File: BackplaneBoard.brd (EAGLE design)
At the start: 139.7 x 79.9 mm, 4 parts

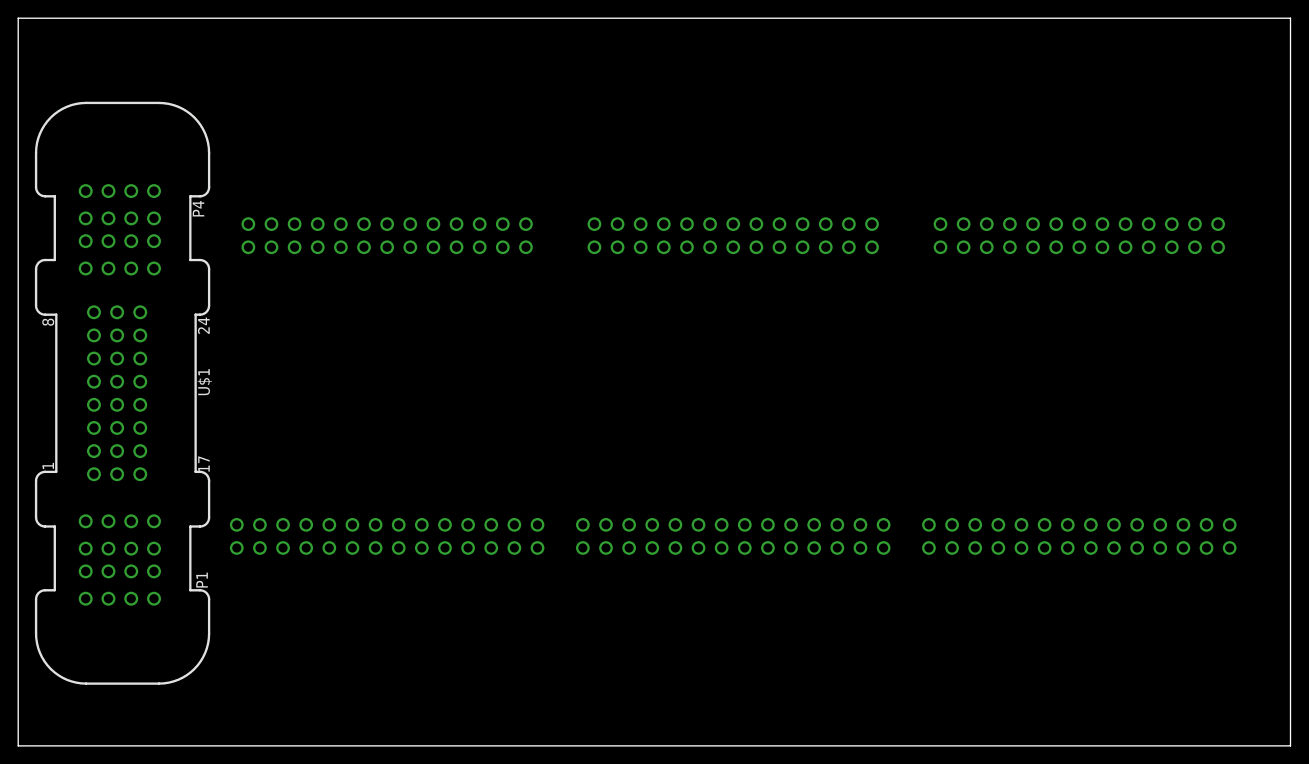
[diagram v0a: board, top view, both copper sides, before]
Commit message: moved some connectors
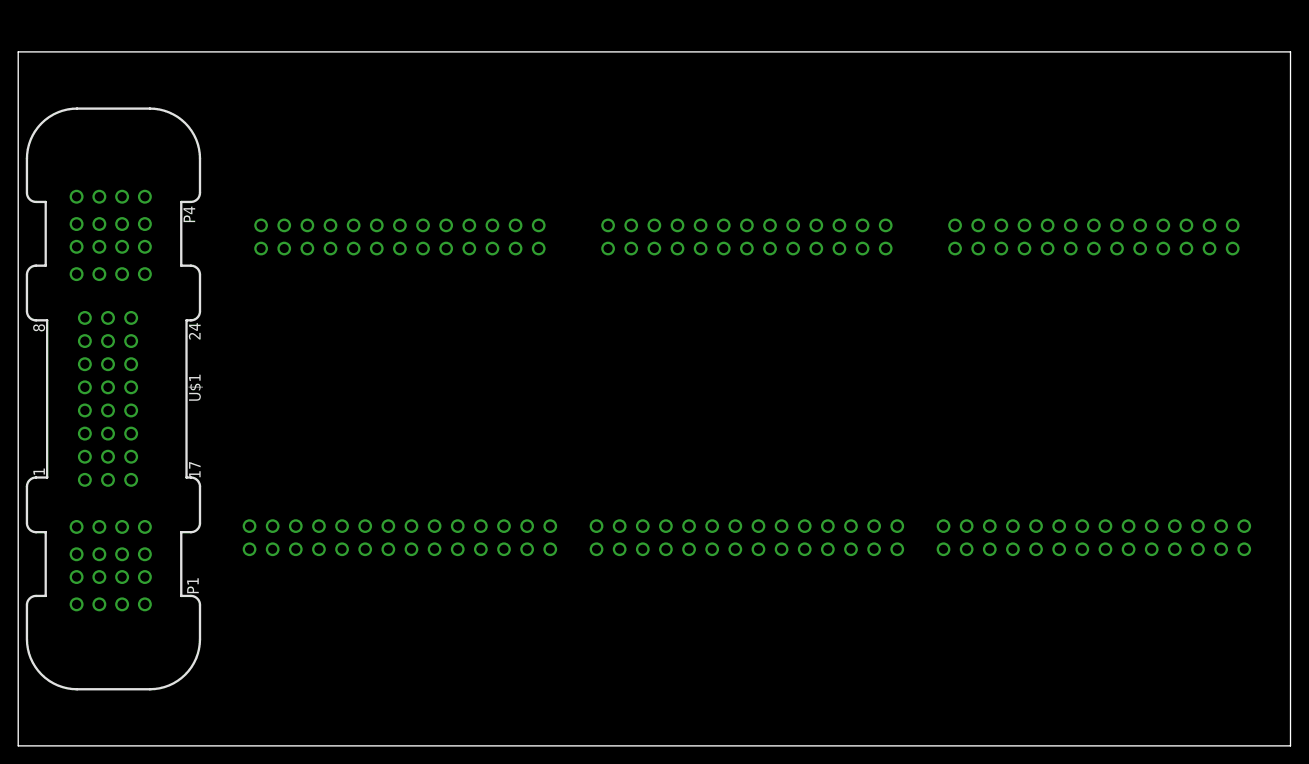
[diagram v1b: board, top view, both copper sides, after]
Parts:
- moved U$4 1.61 mm to (101.6, 22.9)
- moved U$3 1.51 mm to (63.5, 22.9)
- moved U$2 1.41 mm to (25.4, 22.9)
- moved U$1 1.18 mm to (10.2, 38.1)
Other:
- board size 139.7 x 79.9 mm -> 139.7 x 76.2 mm
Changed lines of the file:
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@@
 <setting verticaltext="up"/>
 </settings>
-<grid distance="1" unitdist="mm" unit="mm" style="lines" multiple="1" display="no" altdistance="5" altunitdist="mil" altunit="mil"/>
+<grid distance="1" unitdist="inch" unit="inch" style="lines" multiple="1" display="no" altdistance="5" altunitdist="mil" altunit="mil"/>
 <layers>
 <layer number="1" name="Top" color="4" fill="1" visible="yes" active="yes"/>
@@
 <plain>
 <wire x1="0" y1="0" x2="139.7" y2="0" width="0" layer="20"/>
-<wire x1="139.7" y1="0" x2="139.7" y2="79.9" width="0" layer="20"/>
-<wire x1="139.7" y1="79.9" x2="0" y2="79.9" width="0" layer="20"/>
-<wire x1="0" y1="79.9" x2="0" y2="0" width="0" layer="20"/>
+<wire x1="139.7" y1="0" x2="139.7" y2="76.2" width="0" layer="20"/>
+<wire x1="139.7" y1="76.2" x2="0" y2="76.2" width="0" layer="20"/>
+<wire x1="0" y1="76.2" x2="0" y2="0" width="0" layer="20"/>
 </plain>
 <attributes>
@@
 </autorouter>
 <elements>
-<element name="U$1" library="ET60S-02-24-02-X-VP-GP" package="ET60S-02-24-02-X-VP-GP" value="ET60S-02-24-02-X-VP-GP" x="11.16" y="38.72" rot="R270">
-<attribute name="NAME" x="19.76" y="41.52" size="1.27" layer="25" rot="R270"/>
-<attribute name="VALUE" x="2.56" y="41.52" size="1.27" layer="27" rot="R270"/>
+<element name="U$1" library="ET60S-02-24-02-X-VP-GP" package="ET60S-02-24-02-X-VP-GP" value="ET60S-02-24-02-X-VP-GP" x="10.16" y="38.1" rot="R270">
+<attribute name="NAME" x="18.76" y="40.9" size="1.27" layer="25" rot="R270"/>
+<attribute name="VALUE" x="1.56" y="40.9" size="1.27" layer="27" rot="R270"/>
 </element>
-<element name="U$2" library="ESC_to_Backplane_Connectors" package="ESC2BACKPLANE_WHOLE" value="ESC2BACKPLANE" x="24" y="23"/>
-<element name="U$3" library="ESC_to_Backplane_Connectors" package="ESC2BACKPLANE_WHOLE" value="ESC2BACKPLANE" x="62" y="23"/>
-<element name="U$4" library="ESC_to_Backplane_Connectors" package="ESC2BACKPLANE_WHOLE" value="ESC2BACKPLANE" x="100" y="23"/>
+<element name="U$2" library="ESC_to_Backplane_Connectors" package="ESC2BACKPLANE_WHOLE" value="ESC2BACKPLANE" x="25.4" y="22.86"/>
+<element name="U$3" library="ESC_to_Backplane_Connectors" package="ESC2BACKPLANE_WHOLE" value="ESC2BACKPLANE" x="63.5" y="22.86"/>
+<element name="U$4" library="ESC_to_Backplane_Connectors" package="ESC2BACKPLANE_WHOLE" value="ESC2BACKPLANE" x="101.6" y="22.86"/>
 </elements>
 <signals>

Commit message: added holes for standoffs
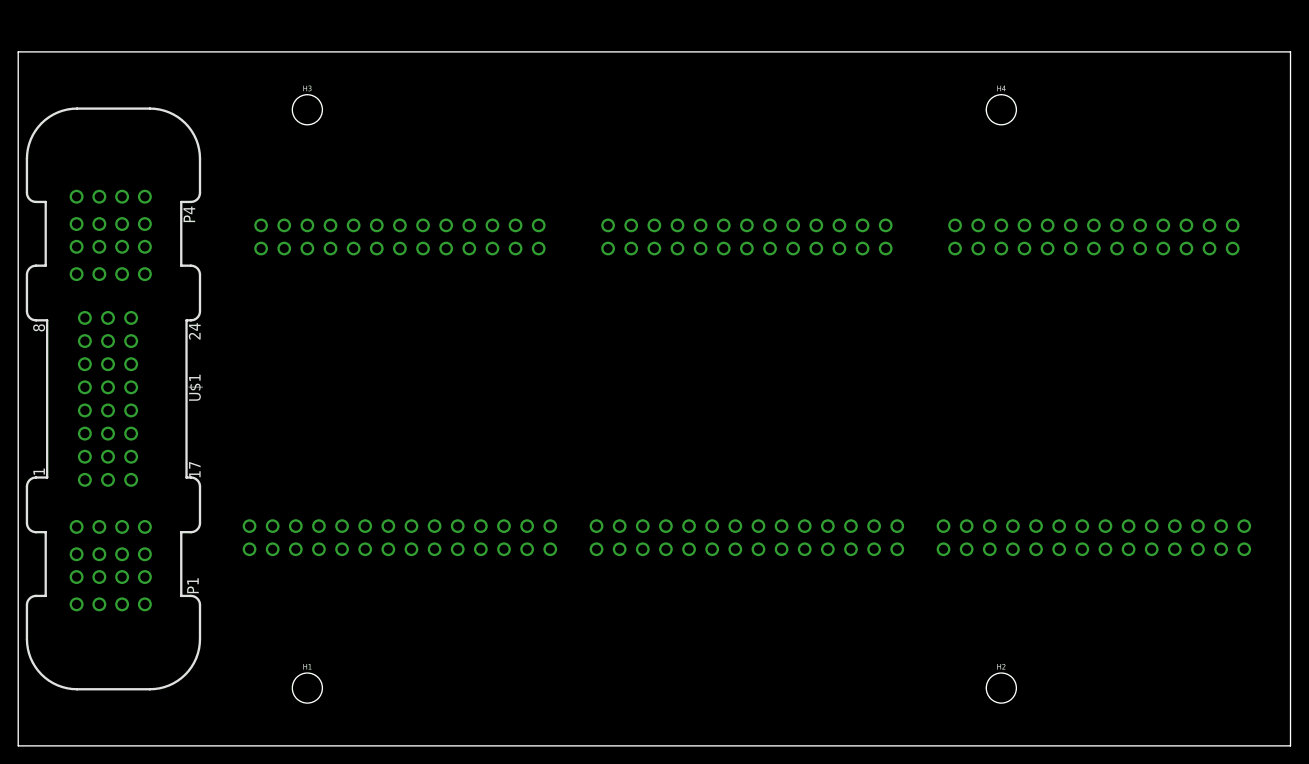
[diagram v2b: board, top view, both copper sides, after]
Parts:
- added H1, H2, H3, H4: STAND-OFF, SparkFun-Hardware:STAND-OFF
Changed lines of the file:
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@@
 <setting verticaltext="up"/>
 </settings>
-<grid distance="1" unitdist="inch" unit="inch" style="lines" multiple="1" display="no" altdistance="5" altunitdist="mil" altunit="mil"/>
+<grid distance="0.75" unitdist="inch" unit="inch" style="lines" multiple="1" display="no" altdistance="5" altunitdist="mil" altunit="mil"/>
 <layers>
 <layer number="1" name="Top" color="4" fill="1" visible="yes" active="yes"/>
+<layer number="2" name="Route2" color="1" fill="3" visible="yes" active="yes"/>
+<layer number="3" name="Route3" color="4" fill="3" visible="yes" active="yes"/>
+<layer number="4" name="Route4" color="1" fill="4" visible="yes" active="yes"/>
+<layer number="5" name="Route5" color="4" fill="4" visible="yes" active="yes"/>
+<layer number="6" name="Route6" color="1" fill="8" visible="yes" active="yes"/>
+<layer number="7" name="Route7" color="4" fill="8" visible="yes" active="yes"/>
+<layer number="8" name="Route8" color="1" fill="2" visible="yes" active="yes"/>
+<layer number="9" name="Route9" color="4" fill="2" visible="yes" active="yes"/>
+<layer number="10" name="Route10" color="1" fill="7" visible="yes" active="yes"/>
+<layer number="11" name="Route11" color="4" fill="7" visible="yes" active="yes"/>
+<layer number="12" name="Route12" color="1" fill="5" visible="yes" active="yes"/>
+<layer number="13" name="Route13" color="4" fill="5" visible="yes" active="yes"/>
+<layer number="14" name="Route14" color="1" fill="6" visible="yes" active="yes"/>
+<layer number="15" name="Route15" color="4" fill="6" visible="yes" active="yes"/>
 <layer number="16" name="Bottom" color="1" fill="1" visible="yes" active="yes"/>
 <layer number="17" name="Pads" color="2" fill="1" visible="yes" active="yes"/>
@@
 <layer number="112" name="tSilk" color="7" fill="1" visible="yes" active="yes"/>
 <layer number="113" name="IDFDebug" color="7" fill="1" visible="yes" active="yes"/>
+<layer number="114" name="Badge_Outline" color="7" fill="1" visible="yes" active="yes"/>
 <layer number="116" name="Patch_BOT" color="9" fill="4" visible="yes" active="yes"/>
 <layer number="118" name="Rect_Pads" color="7" fill="1" visible="yes" active="yes"/>
@@
 <element name="U$3" library="ESC_to_Backplane_Connectors" package="ESC2BACKPLANE_WHOLE" value="ESC2BACKPLANE" x="63.5" y="22.86"/>
 <element name="U$4" library="ESC_to_Backplane_Connectors" package="ESC2BACKPLANE_WHOLE" value="ESC2BACKPLANE" x="101.6" y="22.86"/>
+<element name="H1" library="SparkFun-Hardware" library_urn="urn:adsk.eagle:library:519" package="STAND-OFF" package3d_urn="urn:adsk.eagle:package:38630/1" value="STAND-OFF" x="31.75" y="6.35">
+<attribute name="NAME" x="31.75" y="8.382" size="0.6096" layer="25" font="vector" ratio="20" align="bottom-center"/>
+<attribute name="VALUE" x="31.75" y="4.318" size="0.6096" layer="27" font="vector" ratio="20" align="top-center"/>
+</element>
+<element name="H2" library="SparkFun-Hardware" library_urn="urn:adsk.eagle:library:519" package="STAND-OFF" package3d_urn="urn:adsk.eagle:package:38630/1" value="STAND-OFF" x="107.95" y="6.35">
+<attribute name="NAME" x="107.95" y="8.382" size="0.6096" layer="25" font="vector" ratio="20" align="bottom-center"/>
+<attribute name="VALUE" x="107.95" y="4.318" size="0.6096" layer="27" font="vector" ratio="20" align="top-center"/>
+</element>
+<element name="H3" library="SparkFun-Hardware" library_urn="urn:adsk.eagle:library:519" package="STAND-OFF" package3d_urn="urn:adsk.eagle:package:38630/1" value="STAND-OFF" x="31.75" y="69.85">
+<attribute name="NAME" x="31.75" y="71.882" size="0.6096" layer="25" font="vector" ratio="20" align="bottom-center"/>
+<attribute name="VALUE" x="31.75" y="67.818" size="0.6096" layer="27" font="vector" ratio="20" align="top-center"/>
+</element>
+<element name="H4" library="SparkFun-Hardware" library_urn="urn:adsk.eagle:library:519" package="STAND-OFF" package3d_urn="urn:adsk.eagle:package:38630/1" value="STAND-OFF" x="107.95" y="69.85">
+<attribute name="NAME" x="107.95" y="71.882" size="0.6096" layer="25" font="vector" ratio="20" align="bottom-center"/>
+<attribute name="VALUE" x="107.95" y="67.818" size="0.6096" layer="27" font="vector" ratio="20" align="top-center"/>
+</element>
 </elements>
 <signals>
@@
 </board>
 </drawing>
+<compatibility>
+<note version="8.2" severity="warning">
+Since Version 8.2, EAGLE supports online libraries. The ids
+of those online libraries will not be understood (or retained)
+with this version.
+</note>
+<note version="8.3" severity="warning">
+Since Version 8.3, EAGLE supports URNs for individual library
+assets (packages, symbols, and devices). The URNs of those assets
+will not be understood (or retained) with this version.
+</note>
+<note version="8.3" severity="warning">
+Since Version 8.3, EAGLE supports the association of 3D packages
+with devices in libraries, schematics, and board files. Those 3D
+packages will not be understood (or retained) with this version.
+</note>
+</compatibility>
 </eagle>

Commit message: Netted and labeled pins
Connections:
- new net +12V: U$2.P$10, U$2.P$11, U$2.P$12, U$2.P$13, U$2.P$23, U$2.P$9, U$2.P$A, U$2.P$B, U$2.P$C, U$2.P$D, U$2.P$E, U$2.P$O, U$2.P$P, U$2.P$Q, U$2.P$R, U$2.P$S, U$3.P$10, U$3.P$11, U$3.P$12, U$3.P$13, U$3.P$23, U$3.P$24, U$3.P$25, U$3.P$26, U$3.P$27, U$3.P$9, U$3.P$A, U$3.P$B, U$3.P$C, U$3.P$D, U$3.P$E, U$3.P$O, U$3.P$P, U$3.P$Q, U$3.P$R, U$3.P$S, U$4.P$10, U$4.P$11, U$4.P$12, U$4.P$13, U$4.P$23, U$4.P$24, U$4.P$25, U$4.P$26, U$4.P$27, U$4.P$9, U$4.P$A, U$4.P$B, U$4.P$C, U$4.P$D, U$4.P$E, U$4.P$O, U$4.P$P, U$4.P$Q, U$4.P$R, U$4.P$S
- new net +3V3: U$2.P$G, U$2.P$H, U$2.P$U, U$2.P$V, U$3.P$G, U$3.P$H, U$3.P$U, U$3.P$V, U$4.P$G, U$4.P$H, U$4.P$U, U$4.P$V
- new net CAN_H: U$2.P$6, U$3.P$6, U$4.P$6
- new net CAN_L: U$2.P$7, U$3.P$7, U$4.P$7
- new net GND: U$2.P$1, U$2.P$15, U$2.P$16, U$2.P$17, U$2.P$18, U$2.P$2, U$2.P$3, U$2.P$4, U$2.P$AA, U$2.P$BB, U$2.P$J, U$2.P$K, U$2.P$L, U$2.P$M, U$2.P$N, U$2.P$X, U$2.P$Y, U$2.P$Z, U$3.P$1, U$3.P$15, U$3.P$16, U$3.P$17, U$3.P$18, U$3.P$2, U$3.P$3, U$3.P$4, U$3.P$AA, U$3.P$BB, U$3.P$J, U$3.P$K, U$3.P$L, U$3.P$M, U$3.P$N, U$3.P$X, U$3.P$Y, U$3.P$Z, U$4.P$1, U$4.P$15, U$4.P$16, U$4.P$17, U$4.P$18, U$4.P$2, U$4.P$3, U$4.P$4, U$4.P$AA, U$4.P$BB, U$4.P$J, U$4.P$K, U$4.P$L, U$4.P$M, U$4.P$N, U$4.P$X, U$4.P$Y, U$4.P$Z
- new net N$6: U$2.P$24, U$2.P$25, U$2.P$26, U$2.P$27
- new net PROG_SEL: U$2.P$5, U$3.P$5, U$4.P$5

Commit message: Added polygons to each signal coming from the ESC connecot pins to see placement and corrected a mistake on netting pins
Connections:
- removed net N$6: U$2.P$24, U$2.P$25, U$2.P$26, U$2.P$27
- net +12V: now also U$2.P$24, U$2.P$25, U$2.P$26, U$2.P$27
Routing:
- net GND: track 0.00 -> 137.3 mm
- net +12V: track 0.00 -> 106.7 mm
- net +3V3: track 0.00 -> 30.5 mm
- added copper zone on layer 1, net +12V
- added copper zone on layer 16, net +3V3
- added copper zone on layer 16, net GND
